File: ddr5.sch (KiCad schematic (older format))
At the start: 37 parts, among them U1 MT60B2G8HB-48B_A

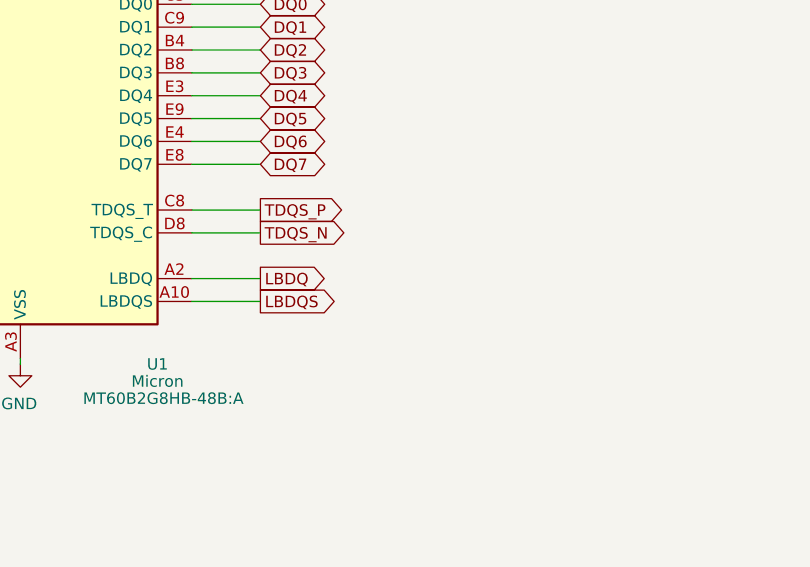
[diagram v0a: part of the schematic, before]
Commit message: Add 0R resistors to LBDQ signals
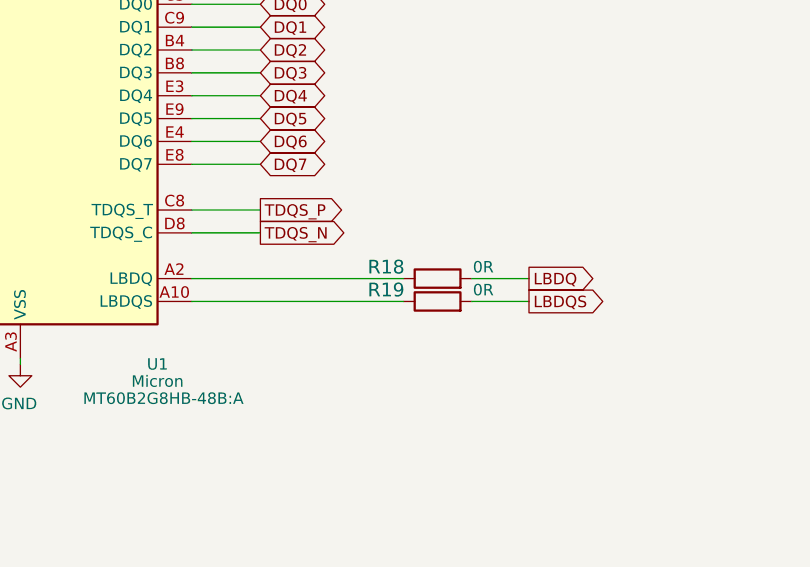
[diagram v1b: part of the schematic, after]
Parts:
- added R18, R19: R_0R_0402, ddr5-testbed-footprints:0402-res, symbol ddr5-testbed:R_0R_0402
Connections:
- net LBDQ: now also R18.2; no longer U1.A2 (LBDQ)
- net LBDQS: now also R19.2; no longer U1.A10 (LBDQS)
- new net: R19.1, U1.A10 (LBDQS)
- new net: R18.1, U1.A2 (LBDQ)
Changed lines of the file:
@@
 	8600 4425 8900 4425
 Wire Wire Line
-	8225 7100 8525 7100
-Text GLabel 8525 7100 2    50   Output ~ 0
-TDQS_P
-Wire Wire Line
-	8225 7200 8525 7200
-Text GLabel 8525 7200 2    50   Output ~ 0
-TDQS_N
-Wire Wire Line
 	6725 7100 6425 7100
 Text GLabel 6425 7100 0    50   BiDi ~ 0
@@
 Wire Wire Line
 	5900 5400 6725 5400
-Wire Wire Line
-	8225 7400 8525 7400
-Text GLabel 8525 7400 2    50   Output ~ 0
+Text GLabel 9700 7400 2    50   Output ~ 0
 LBDQ
-Wire Wire Line
-	8225 7500 8525 7500
-Text GLabel 8525 7500 2    50   Output ~ 0
+Text GLabel 9700 7500 2    50   Output ~ 0
 LBDQS
 Wire Wire Line
@@
 	1    0    0    -1
 $EndComp
+$Comp
+L ddr5-testbed:R_0R_0402 R19
+U 1 1 628003FC
+P 9300 7500
+F 0 "R19" H 9075 7550 60  0000 C CNN
+F 1 "R_0R_0402" H 9300 7350 60  0001 C CNN
+F 2 "ddr5-testbed-footprints:0402-res" H 9500 7700 60  0001 L CNN
+F 3 "" H 9300 7500 50  0001 C CNN
+F 4 "PANASONIC" H 9500 7900 60  0001 L CNN "Manufacturer"
+F 5 "ERJ2GE0R00X" H 9500 7800 60  0001 L CNN "MPN"
+F 6 "0R" H 9500 7550 50  0000 C CNN "Val"
+	1    9300 7500
+	1    0    0    -1
+$EndComp
+$Comp
+L ddr5-testbed:R_0R_0402 R18
+U 1 1 62800405
+P 9300 7400
+F 0 "R18" H 9075 7450 60  0000 C CNN
+F 1 "R_0R_0402" H 9300 7250 60  0001 C CNN
+F 2 "ddr5-testbed-footprints:0402-res" H 9500 7600 60  0001 L CNN
+F 3 "" H 9300 7400 50  0001 C CNN
+F 4 "PANASONIC" H 9500 7800 60  0001 L CNN "Manufacturer"
+F 5 "ERJ2GE0R00X" H 9500 7700 60  0001 L CNN "MPN"
+F 6 "0R" H 9500 7450 50  0000 C CNN "Val"
+	1    9300 7400
+	1    0    0    -1
+$EndComp
+Wire Wire Line
+	8225 7400 9150 7400
+Wire Wire Line
+	8225 7500 9150 7500
+Wire Wire Line
+	9700 7400 9450 7400
+Wire Wire Line
+	9450 7500 9700 7500
+Wire Wire Line
+	8225 7200 8525 7200
+Wire Wire Line
+	8225 7100 8525 7100
+Text GLabel 8525 7200 2    50   Output ~ 0
+TDQS_N
+Text GLabel 8525 7100 2    50   Output ~ 0
+TDQS_P
 $EndSCHEMATC

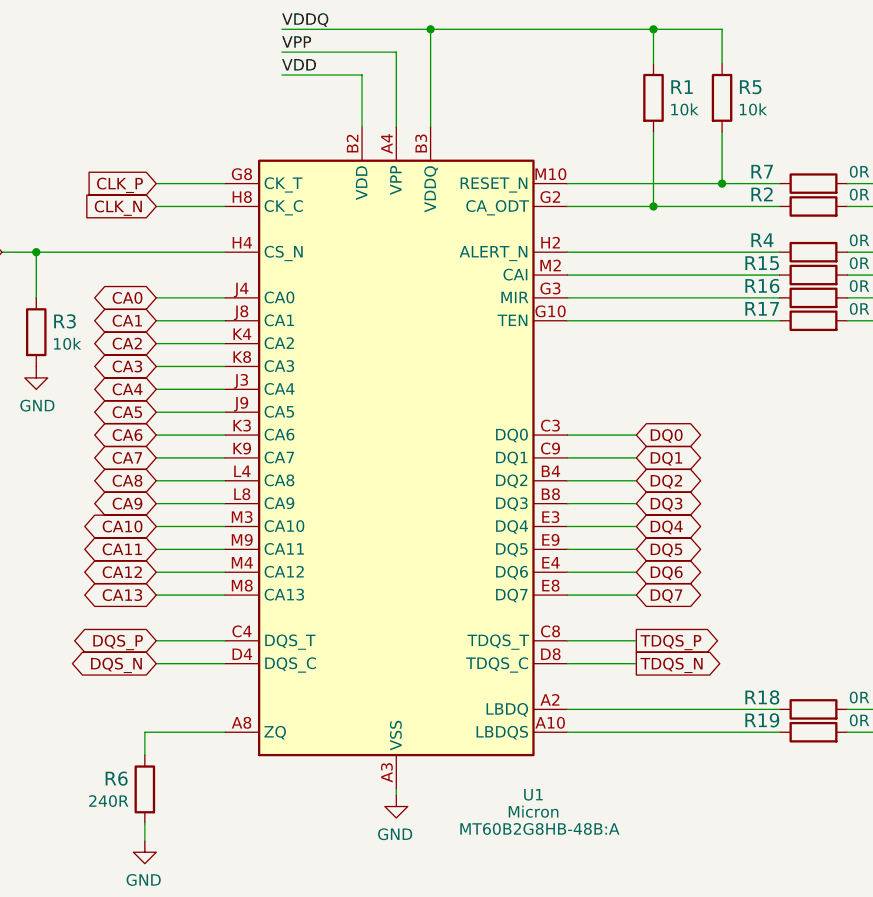
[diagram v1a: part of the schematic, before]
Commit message: Add signal labels to SCH
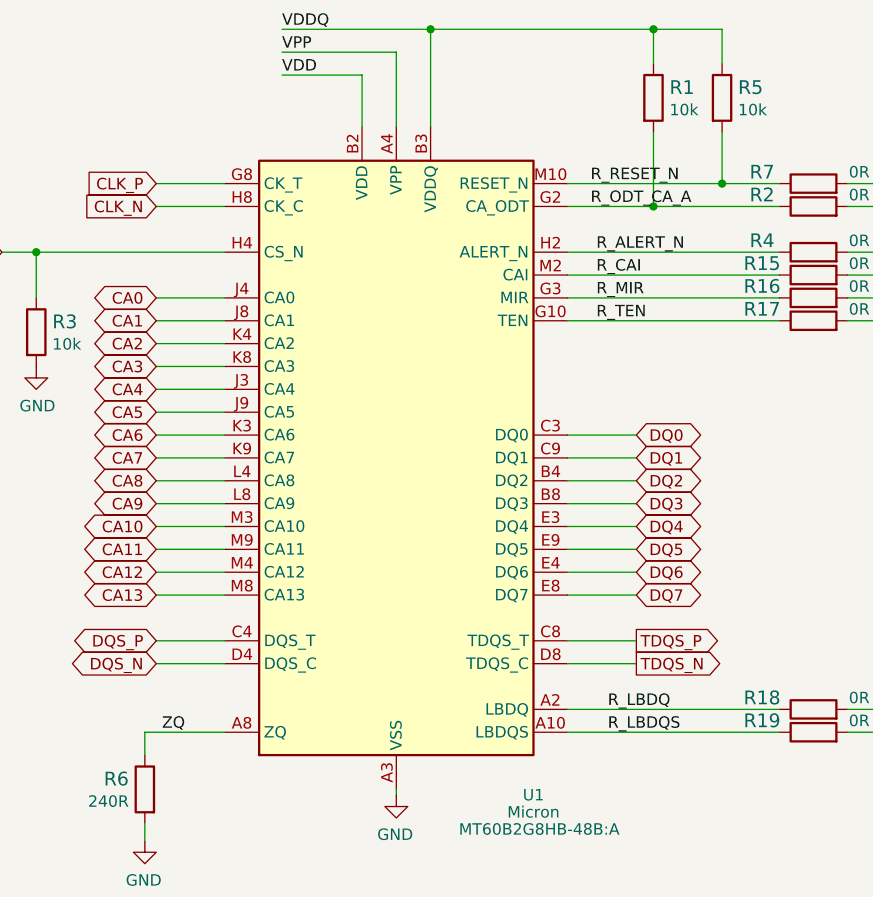
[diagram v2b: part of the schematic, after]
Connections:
- net R_ODT_CA_A: now reaches R1.2, R2.1, U1.G2 (CA_ODT)
- net R_RESET_N: now reaches R5.2, R7.1, U1.M10 (RESET_N)
- net ZQ: now reaches R6.1, U1.A8 (ZQ)
- net R_LBDQS: now reaches R19.1, U1.A10 (LBDQS)
- net R_LBDQ: now reaches R18.1, U1.A2 (LBDQ)
- net R_TEN: now reaches R17.1, U1.G10 (TEN)
- net R_MIR: now reaches R16.1, U1.G3 (MIR)
- net R_ALERT_N: now reaches R4.1, U1.H2 (ALERT_N)
- net R_CAI: now reaches R15.1, U1.M2 (CAI)
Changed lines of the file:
@@
 Text GLabel 8525 7100 2    50   Output ~ 0
 TDQS_P
+Text Label 8350 5400 0    50   ~ 0
+R_ALERT_N
+Text Label 8350 5500 0    50   ~ 0
+R_CAI
+Text Label 8350 5600 0    50   ~ 0
+R_MIR
+Text Label 8350 5700 0    50   ~ 0
+R_TEN
+Text Label 8325 5100 0    50   ~ 0
+R_RESET_N
+Text Label 8325 5200 0    50   ~ 0
+R_ODT_CA_A
+Text Label 6450 7500 0    50   ~ 0
+ZQ
+Text Label 8400 7400 0    50   ~ 0
+R_LBDQ
+Text Label 8400 7500 0    50   ~ 0
+R_LBDQS
 $EndSCHEMATC

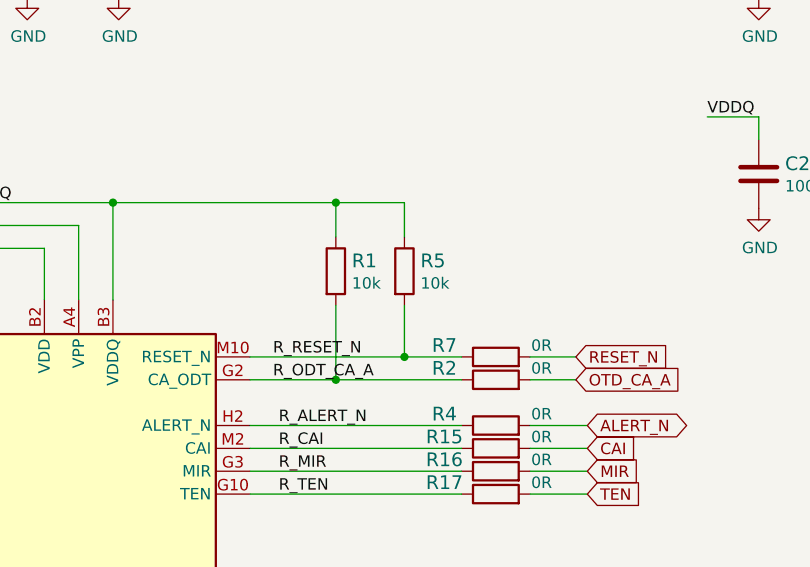
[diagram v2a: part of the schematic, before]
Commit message: Change pullup resistors to 1K
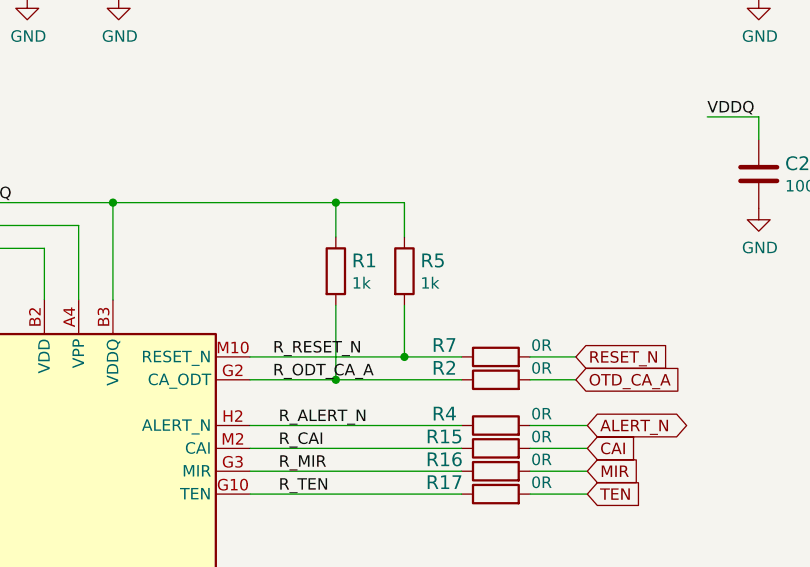
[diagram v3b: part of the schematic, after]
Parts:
- removed R1, R5: R_10k_0402, ddr5-testbed-footprints:0402-res, symbol ddr5-testbed:R_10k_0402
- added R1, R5: R_1k_0402, ddr5-testbed-footprints:0402-res, symbol ddr5-testbed:R_1k_0402
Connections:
- net R_ODT_CA_A: now also R1.2
- net R_RESET_N: now also R5.2
- net VDDQ: now also R1.1, R5.1
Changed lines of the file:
@@
 	5900 5600 5900 5400
 Connection ~ 5900 5400
-$Comp
-L ddr5-testbed:R_10k_0402 R1
-U 1 1 5FD814A6
-P 8600 4725
-F 0 "R1" V 8555 4795 60  0000 L CNN
-F 1 "R_10k_0402" H 8600 4575 60  0001 C CNN
-F 2 "ddr5-testbed-footprints:0402-res" H 8800 4925 60  0001 L CNN
-F 3 "" H 8600 4725 50  0001 C CNN
-F 4 "VISHAY" H 8800 5125 60  0001 L CNN "Manufacturer"
-F 5 "CRCW040210K0FKEDHP" H 8800 5025 60  0001 L CNN "MPN"
-F 6 "10k" V 8653 4795 50  0000 L CNN "Val"
-	1    8600 4725
-	0    1    1    0
-$EndComp
 Wire Wire Line
 	8600 4875 8600 5200
@@
 Wire Wire Line
 	9450 5200 9650 5200
-$Comp
-L ddr5-testbed:R_10k_0402 R5
-U 1 1 5FFC8223
-P 8900 4725
-F 0 "R5" V 8855 4795 60  0000 L CNN
-F 1 "R_10k_0402" H 8900 4575 60  0001 C CNN
-F 2 "ddr5-testbed-footprints:0402-res" H 9100 4925 60  0001 L CNN
-F 3 "" H 8900 4725 50  0001 C CNN
-F 4 "VISHAY" H 9100 5125 60  0001 L CNN "Manufacturer"
-F 5 "CRCW040210K0FKEDHP" H 9100 5025 60  0001 L CNN "MPN"
-F 6 "10k" V 8953 4795 50  0000 L CNN "Val"
-	1    8900 4725
-	0    1    1    0
-$EndComp
 Wire Wire Line
 	8225 5100 8900 5100
@@
 Text Label 8400 7500 0    50   ~ 0
 R_LBDQS
+$Comp
+L ddr5-testbed:R_1k_0402 R1
+U 1 1 624D8485
+P 8600 4725
+F 0 "R1" V 8555 4795 60  0000 L CNN
+F 1 "R_1k_0402" H 8600 4575 60  0001 C CNN
+F 2 "ddr5-testbed-footprints:0402-res" H 8800 4925 60  0001 L CNN
+F 3 "" H 8600 4725 50  0001 C CNN
+F 4 "BOURNS" H 8800 5125 60  0001 L CNN "Manufacturer"
+F 5 "CR0402-FX-1001GLF" H 8800 5025 60  0001 L CNN "MPN"
+F 6 "1k" V 8653 4795 50  0000 L CNN "Val"
+	1    8600 4725
+	0    1    1    0
+$EndComp
+$Comp
+L ddr5-testbed:R_1k_0402 R5
+U 1 1 624DA599
+P 8900 4725
+F 0 "R5" V 8855 4795 60  0000 L CNN
+F 1 "R_1k_0402" H 8900 4575 60  0001 C CNN
+F 2 "ddr5-testbed-footprints:0402-res" H 9100 4925 60  0001 L CNN
+F 3 "" H 8900 4725 50  0001 C CNN
+F 4 "BOURNS" H 9100 5125 60  0001 L CNN "Manufacturer"
+F 5 "CR0402-FX-1001GLF" H 9100 5025 60  0001 L CNN "MPN"
+F 6 "1k" V 8953 4795 50  0000 L CNN "Val"
+	1    8900 4725
+	0    1    1    0
+$EndComp
 $EndSCHEMATC

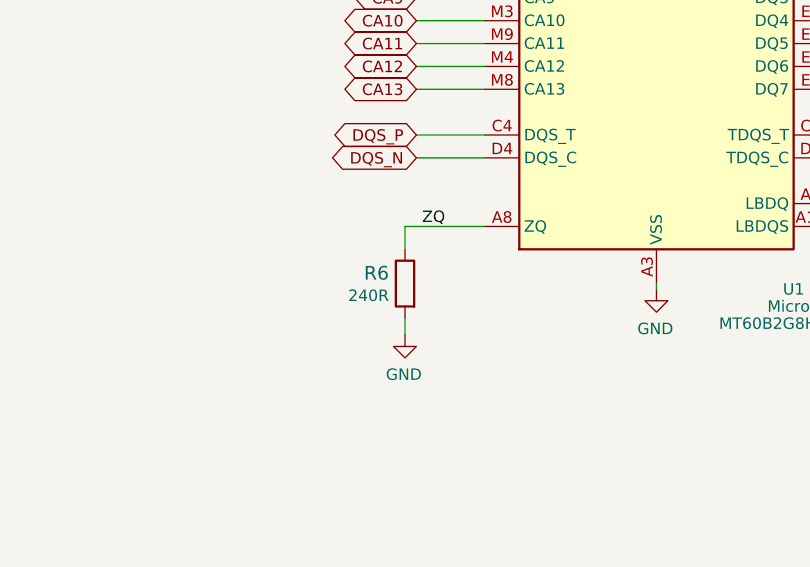
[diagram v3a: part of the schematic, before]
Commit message: Change R6 to 1% tolerance
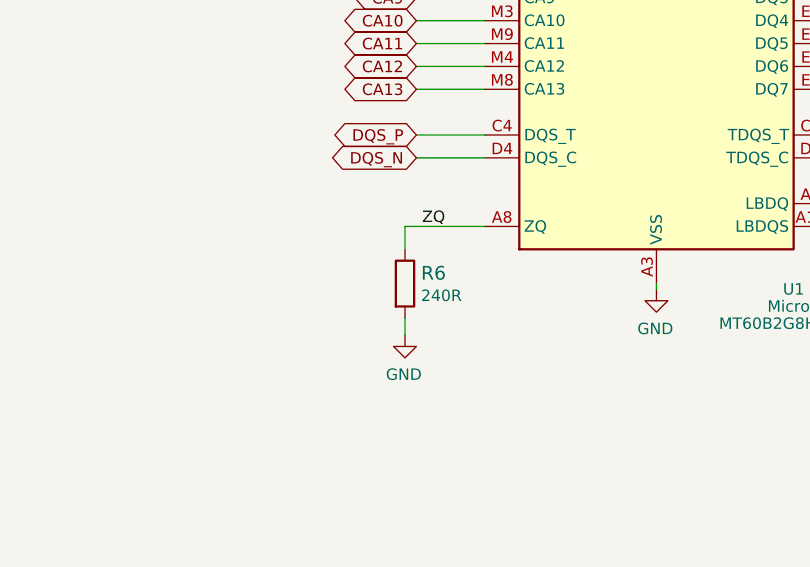
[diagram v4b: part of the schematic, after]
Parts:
- removed R6: R_240R_0402, ddr5-testbed-footprints:0402-res, symbol ddr5-testbed:R_240R_0402
- added R6: R_240R_1%_0402, ddr5-testbed-footprints:0402-res, symbol ddr5-testbed:R_240R_1%_0402
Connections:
- net GND: now also R6.2
- net ZQ: now also R6.1
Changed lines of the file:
@@
 	9450 5100 9650 5100
 $Comp
-L ddr5-testbed:R_240R_0402 R6
-U 1 1 600C5846
-P 6375 7750
-F 0 "R6" V 6330 7820 60  0000 L CNN
-F 1 "R_240R_0402" H 6375 7600 60  0001 C CNN
-F 2 "ddr5-testbed-footprints:0402-res" H 6575 7950 60  0001 L CNN
-F 3 "" H 6375 7750 50  0001 C CNN
-F 4 "PANASONIC" H 6575 8150 60  0001 L CNN "Manufacturer"
-F 5 "ERJ2GEJ241X" H 6575 8050 60  0001 L CNN "MPN"
-F 6 "240R" V 6428 7820 50  0000 L CNN "Val"
-	1    6375 7750
-	0    -1   1    0
-$EndComp
-$Comp
 L ddr5-testbed:GND #PWR0105
 U 1 1 600C5DD3
@@
 	0    1    1    0
 $EndComp
+$Comp
+L ddr5-testbed:R_240R_1%_0402 R6
+U 1 1 6254452D
+P 6375 7750
+F 0 "R6" V 6330 7820 60  0000 L CNN
+F 1 "R_240R_1%_0402" H 6375 7600 60  0001 C CNN
+F 2 "ddr5-testbed-footprints:0402-res" H 6575 7950 60  0001 L CNN
+F 3 "" H 6375 7750 50  0001 C CNN
+F 4 "Yageo" H 6575 8150 60  0001 L CNN "Manufacturer"
+F 5 "RC0402FR-13240RL" H 6575 8050 60  0001 L CNN "MPN"
+F 6 "240R" V 6428 7820 50  0000 L CNN "Val"
+	1    6375 7750
+	0    1    1    0
+$EndComp

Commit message: Assign schematic labels
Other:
- note added: "DDR5 DRAM IC"
- note removed: "LPDDR4"
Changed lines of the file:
@@
 Title "DDR5 testbed"
 Date "2022-03-02"
-Rev "1.0.0"
+Rev "1.0.1"
 Comp ""
 Comment1 ""
@@
 $EndDescr
 Text Notes 1075 1025 0    98   ~ 20
-LPDDR4
+DDR5 DRAM IC
 Wire Notes Line
 	4700 11175 4675 11175
